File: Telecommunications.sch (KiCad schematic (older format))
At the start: 15 parts, among them J1 U_FL-R-SMT_10_, J2 142-0701-801, J3 142-0701-801, U1 E22-900M30S, U4 NEO-M8N

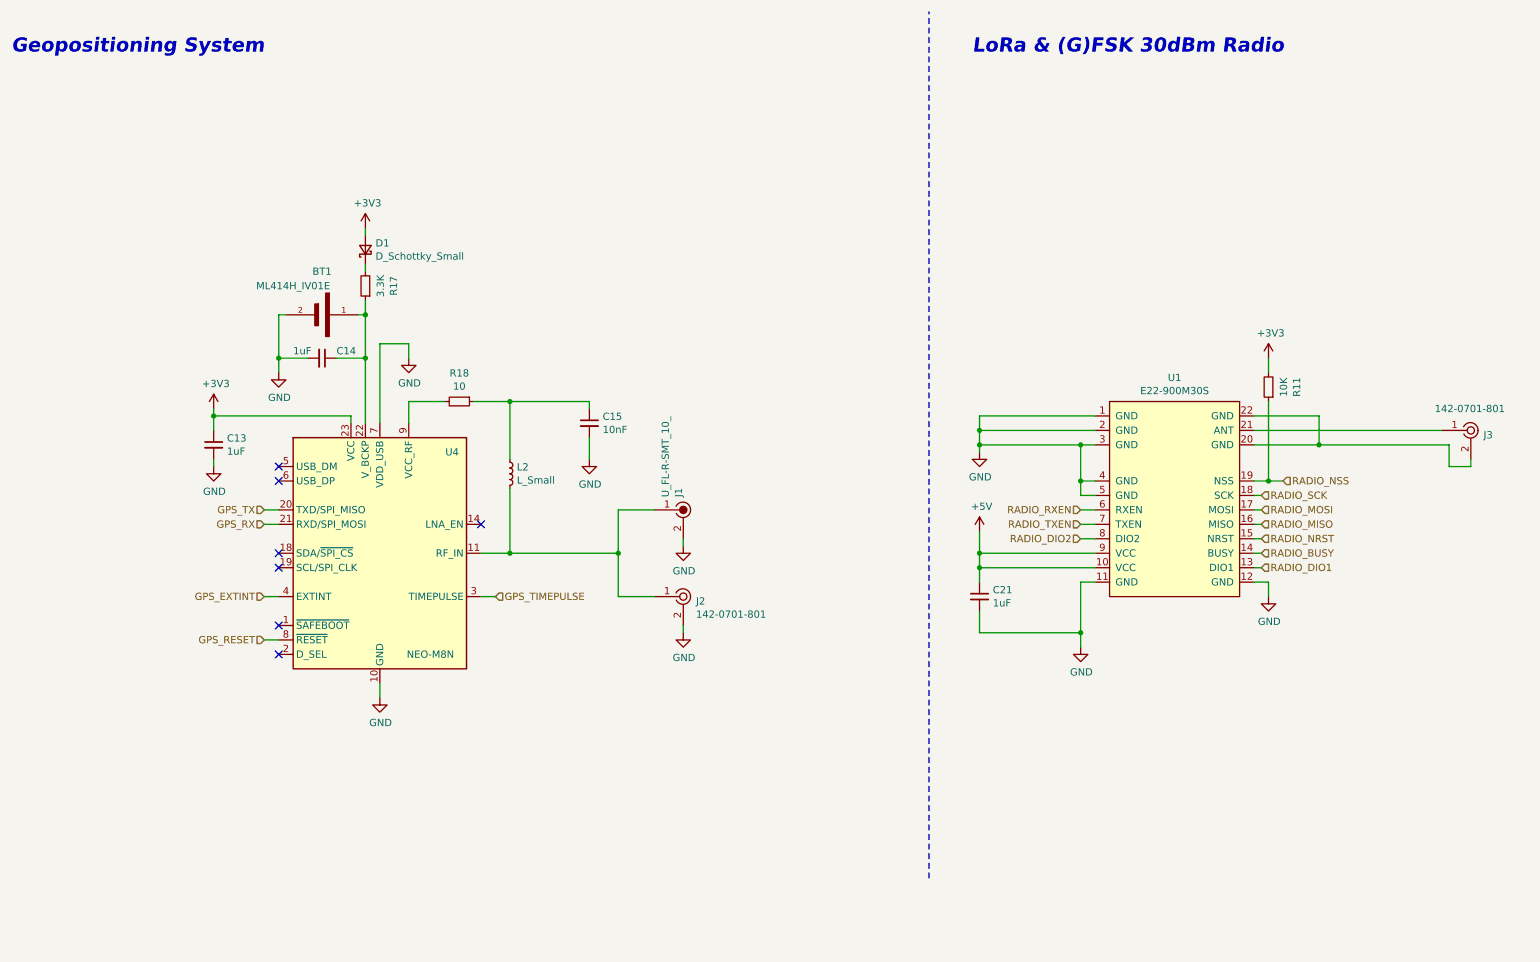
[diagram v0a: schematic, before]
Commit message: Updated silk screens and components 3D models
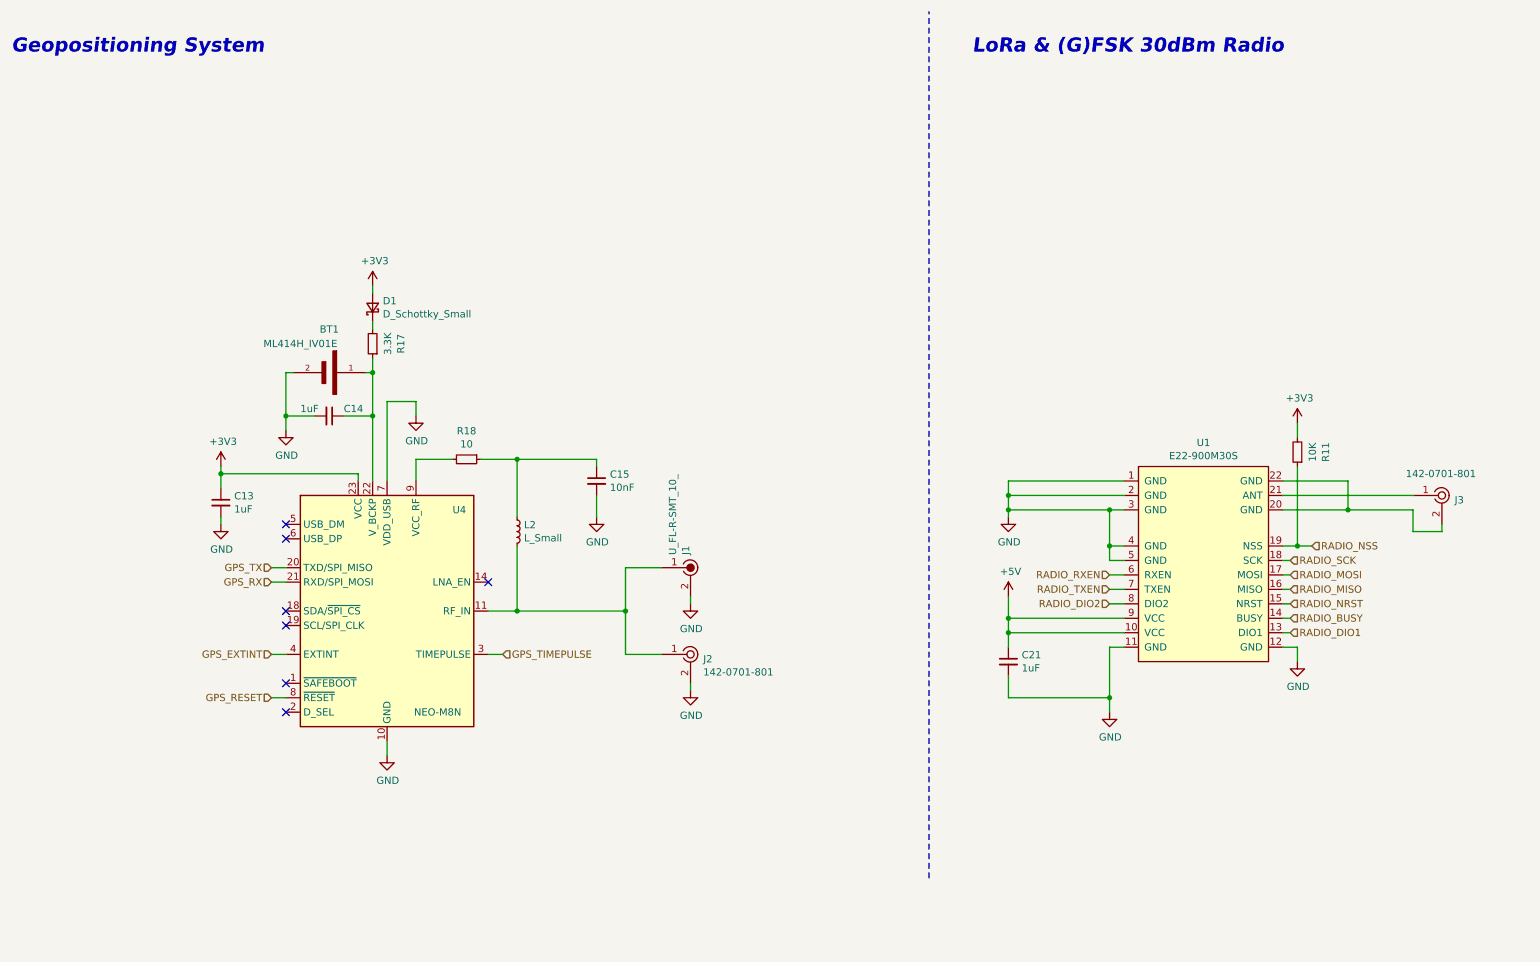
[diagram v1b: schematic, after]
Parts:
- L2: footprint Inductor_SMD:L_0805_2012Metric_Pad1.15x1.40mm_HandSolder -> Inductor_SMD:L_0402_1005Metric_Pad0.77x0.64mm_HandSolder
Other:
- moved on the sheet: BT1, C13, C14, C15, C21, D1, J1, J2, J3, L2, R11, R17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

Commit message: Updated RF section ground planes.
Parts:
- added Q7: 2N7002NXAKR, SamacSys_Parts:SOT95P230X110-3N, symbol SamacSys_Parts:2N7002NXAKR
- added R33: 330, Resistor_SMD:R_0603_1608Metric, symbol Device:R_Small
- added R34: 10K, Resistor_SMD:R_0603_1608Metric, symbol Device:R_Small
- U4: symbol RF_GPS:NEO-M8N -> Zenith_Modified_Libraries:NEO-M8N
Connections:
- net GND: now also Q7.2, R34.1; no longer C15.2, J1.2, J2.2, U4.10 (GND), U4.12 (GND), U4.13 (GND), U4.24 (GND), U4.7 (VDD_USB)
- net GPS_TIMEPULSE: no longer names the net of U4.3 (TIMEPULSE)
- new net: Q7.1, R33.2, R34.2
- new net GND1: Q7.3, U4.13 (GND), U4.24 (GND), U4.7 (VDD_USB)
- new net GNDA: C15.2, J1.2, J2.2, U4.10 (GND), U4.12 (GND)
- new net GPS_ON_OFF: R33.1
- no-connect marks 7 -> 8
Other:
- moved on the sheet: C15, J1, J2, L2
